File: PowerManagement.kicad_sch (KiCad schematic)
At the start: 6 parts

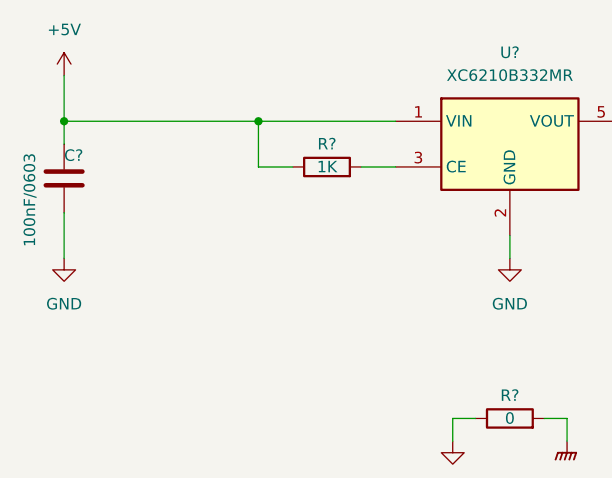
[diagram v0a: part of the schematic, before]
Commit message: Add IO sub schematic, add communications
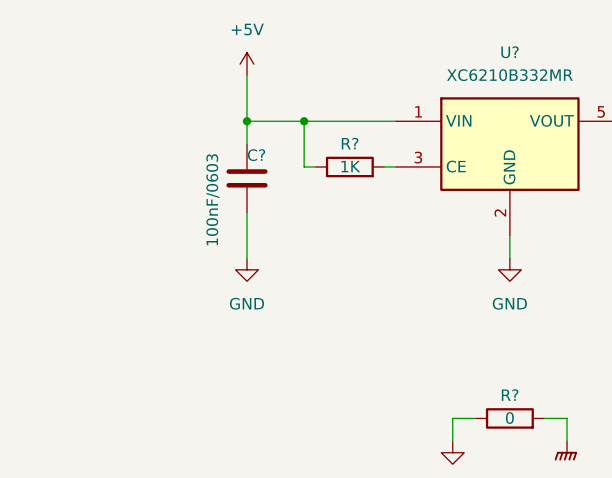
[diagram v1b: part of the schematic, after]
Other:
- moved on the sheet: C?, R?
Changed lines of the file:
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@@
   (junction (at 158.75 93.98) (diameter 0) (color 0 0 0 0)
   )
-  (junction (at 91.44 93.98) (diameter 0) (color 0 0 0 0)
-  )
-  (junction (at 113.03 93.98) (diameter 0) (color 0 0 0 0)
-  )
-  (wire (pts (xy 91.44 93.98) (xy 91.44 96.52))
-    (stroke (width 0) (type default) (color 0 0 0 0))
-  )
-  (wire (pts (xy 116.84 99.06) (xy 113.03 99.06))
+  (junction (at 111.76 93.98) (diameter 0) (color 0 0 0 0)
+  )
+  (junction (at 118.11 93.98) (diameter 0) (color 0 0 0 0)
+  )
+  (wire (pts (xy 111.76 93.98) (xy 111.76 96.52))
+    (stroke (width 0) (type default) (color 0 0 0 0))
+  )
+  (wire (pts (xy 119.38 99.06) (xy 118.11 99.06))
+    (stroke (width 0) (type default) (color 0 0 0 0))
+  )
+  (wire (pts (xy 118.11 93.98) (xy 128.27 93.98))
     (stroke (width 0) (type default) (color 0 0 0 0))
   )
@@
     (stroke (width 0) (type default) (color 0 0 0 0))
   )
-  (wire (pts (xy 113.03 99.06) (xy 113.03 93.98))
+  (wire (pts (xy 118.11 99.06) (xy 118.11 93.98))
     (stroke (width 0) (type default) (color 0 0 0 0))
   )
@@
     (stroke (width 0) (type default) (color 0 0 0 0))
   )
-  (wire (pts (xy 91.44 93.98) (xy 113.03 93.98))
-    (stroke (width 0) (type default) (color 0 0 0 0))
-  )
-  (wire (pts (xy 124.46 99.06) (xy 128.27 99.06))
+  (wire (pts (xy 111.76 93.98) (xy 118.11 93.98))
+    (stroke (width 0) (type default) (color 0 0 0 0))
+  )
+  (wire (pts (xy 127 99.06) (xy 128.27 99.06))
     (stroke (width 0) (type default) (color 0 0 0 0))
   )
@@
     (stroke (width 0) (type default) (color 0 0 0 0))
   )
-  (wire (pts (xy 113.03 93.98) (xy 128.27 93.98))
-    (stroke (width 0) (type default) (color 0 0 0 0))
-  )
   (wire (pts (xy 158.75 104.14) (xy 158.75 109.22))
     (stroke (width 0) (type default) (color 0 0 0 0))
@@
     (stroke (width 0) (type default) (color 0 0 0 0))
   )
-  (wire (pts (xy 91.44 88.9) (xy 91.44 93.98))
-    (stroke (width 0) (type default) (color 0 0 0 0))
-  )
-  (wire (pts (xy 91.44 104.14) (xy 91.44 109.22))
+  (wire (pts (xy 111.76 88.9) (xy 111.76 93.98))
+    (stroke (width 0) (type default) (color 0 0 0 0))
+  )
+  (wire (pts (xy 111.76 104.14) (xy 111.76 109.22))
     (stroke (width 0) (type default) (color 0 0 0 0))
   )
@@
     (pin "1")
   )
-  (symbol (lib_id "power:+5V") (at 91.44 88.9 0) (unit 1)
-    (in_bom yes) (on_board yes) (fields_autoplaced)
-    (property "Reference" "#PWR?" (id 0) (at 91.44 92.71 0)
-      (effects (font (size 1.27 1.27)) hide)
-    )
-    (property "Value" "+5V" (id 1) (at 91.44 83.82 0))
-    (property "Footprint" "" (id 2) (at 91.44 88.9 0)
-      (effects (font (size 1.27 1.27)) hide)
-    )
-    (property "Datasheet" "" (id 3) (at 91.44 88.9 0)
+  (symbol (lib_id "power:+5V") (at 111.76 88.9 0) (unit 1)
+    (in_bom yes) (on_board yes) (fields_autoplaced)
+    (property "Reference" "#PWR?" (id 0) (at 111.76 92.71 0)
+      (effects (font (size 1.27 1.27)) hide)
+    )
+    (property "Value" "+5V" (id 1) (at 111.76 83.82 0))
+    (property "Footprint" "" (id 2) (at 111.76 88.9 0)
+      (effects (font (size 1.27 1.27)) hide)
+    )
+    (property "Datasheet" "" (id 3) (at 111.76 88.9 0)
       (effects (font (size 1.27 1.27)) hide)
     )
@@
     (pin "2")
   )
-  (symbol (lib_id "Device:C") (at 91.44 100.33 180) (unit 1)
-    (in_bom yes) (on_board yes)
-    (property "Reference" "C?" (id 0) (at 91.44 97.79 0)
-      (effects (font (size 1.27 1.27)) (justify right))
-    )
-    (property "Value" "100nF/0603" (id 1) (at 87.63 107.95 90)
-      (effects (font (size 1.27 1.27)) (justify right))
-    )
-    (property "Footprint" "Capacitor_SMD:C_0603_1608Metric" (id 2) (at 90.4748 96.52 0)
-      (effects (font (size 1.27 1.27)) hide)
-    )
-    (property "Datasheet" "~" (id 3) (at 91.44 100.33 0)
-      (effects (font (size 1.27 1.27)) hide)
-    )
-    (pin "1")
-    (pin "2")
-  )
-  (symbol (lib_id "power:GND") (at 91.44 109.22 0) (unit 1)
-    (in_bom yes) (on_board yes) (fields_autoplaced)
-    (property "Reference" "#PWR?" (id 0) (at 91.44 115.57 0)
-      (effects (font (size 1.27 1.27)) hide)
-    )
-    (property "Value" "GND" (id 1) (at 91.44 114.3 0))
-    (property "Footprint" "" (id 2) (at 91.44 109.22 0)
-      (effects (font (size 1.27 1.27)) hide)
-    )
-    (property "Datasheet" "" (id 3) (at 91.44 109.22 0)
+  (symbol (lib_id "Device:C") (at 111.76 100.33 180) (unit 1)
+    (in_bom yes) (on_board yes)
+    (property "Reference" "C?" (id 0) (at 111.76 97.79 0)
+      (effects (font (size 1.27 1.27)) (justify right))
+    )
+    (property "Value" "100nF/0603" (id 1) (at 107.95 107.95 90)
+      (effects (font (size 1.27 1.27)) (justify right))
+    )
+    (property "Footprint" "Capacitor_SMD:C_0603_1608Metric" (id 2) (at 110.7948 96.52 0)
+      (effects (font (size 1.27 1.27)) hide)
+    )
+    (property "Datasheet" "~" (id 3) (at 111.76 100.33 0)
+      (effects (font (size 1.27 1.27)) hide)
+    )
+    (pin "1")
+    (pin "2")
+  )
+  (symbol (lib_id "power:GND") (at 111.76 109.22 0) (unit 1)
+    (in_bom yes) (on_board yes) (fields_autoplaced)
+    (property "Reference" "#PWR?" (id 0) (at 111.76 115.57 0)
+      (effects (font (size 1.27 1.27)) hide)
+    )
+    (property "Value" "GND" (id 1) (at 111.76 114.3 0))
+    (property "Footprint" "" (id 2) (at 111.76 109.22 0)
+      (effects (font (size 1.27 1.27)) hide)
+    )
+    (property "Datasheet" "" (id 3) (at 111.76 109.22 0)
       (effects (font (size 1.27 1.27)) hide)
     )
@@
     (pin "5")
   )
-  (symbol (lib_id "Device:R") (at 120.65 99.06 90) (unit 1)
-    (in_bom yes) (on_board yes)
-    (property "Reference" "R?" (id 0) (at 120.65 96.52 90))
-    (property "Value" "1K" (id 1) (at 120.65 99.06 90))
-    (property "Footprint" "Resistor_SMD:R_0603_1608Metric" (id 2) (at 120.65 100.838 90)
-      (effects (font (size 1.27 1.27)) hide)
-    )
-    (property "Datasheet" "~" (id 3) (at 120.65 99.06 0)
-      (effects (font (size 1.27 1.27)) hide)
-    )
+  (symbol (lib_id "Device:R") (at 123.19 99.06 90) (unit 1)
+    (in_bom yes) (on_board yes)
+    (property "Reference" "R?" (id 0) (at 123.19 96.52 90))
+    (property "Value" "1K" (id 1) (at 123.19 99.06 90))
+    (property "Footprint" "Resistor_SMD:R_0603_1608Metric" (id 2) (at 123.19 100.838 90)
+      (effects (font (size 1.27 1.27)) hide)
+    )
+    (property "Datasheet" "~" (id 3) (at 123.19 99.06 0)
+      (effects (font (size 1.27 1.27)) hide)
+    )

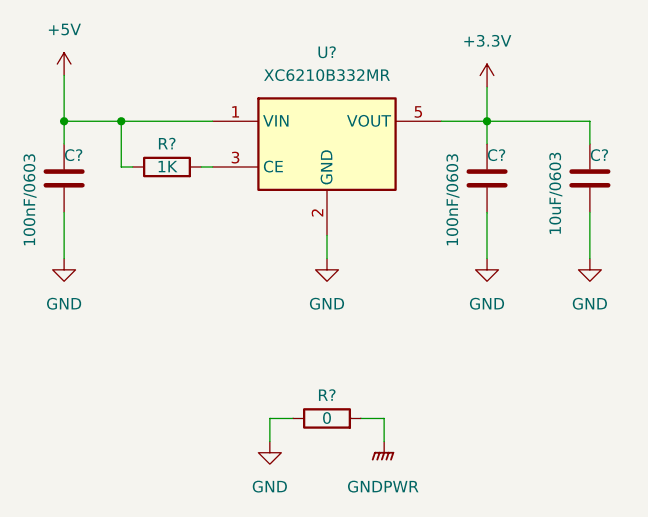
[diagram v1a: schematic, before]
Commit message: add IO, MCU, power sheets
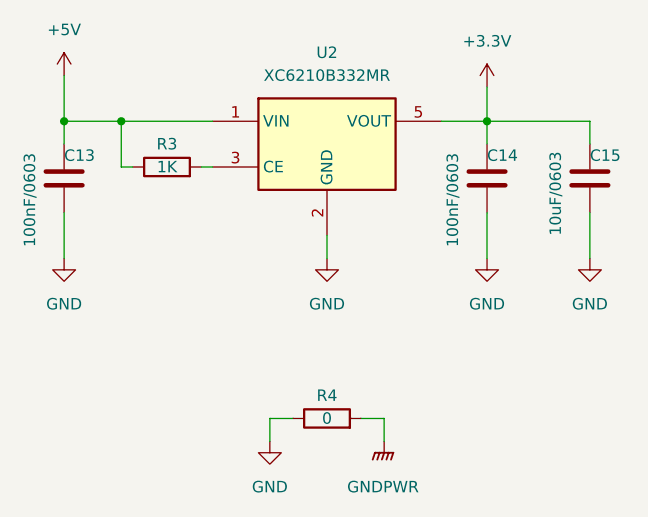
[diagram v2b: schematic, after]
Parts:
- gave numbers to parts that had none: 6

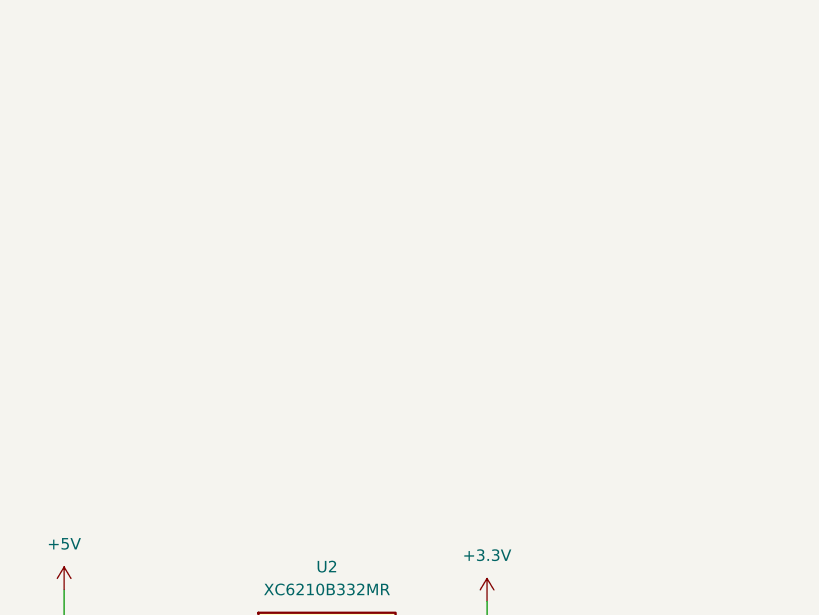
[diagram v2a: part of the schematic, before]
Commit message: Add buck converter, add part of pinmap to mcu
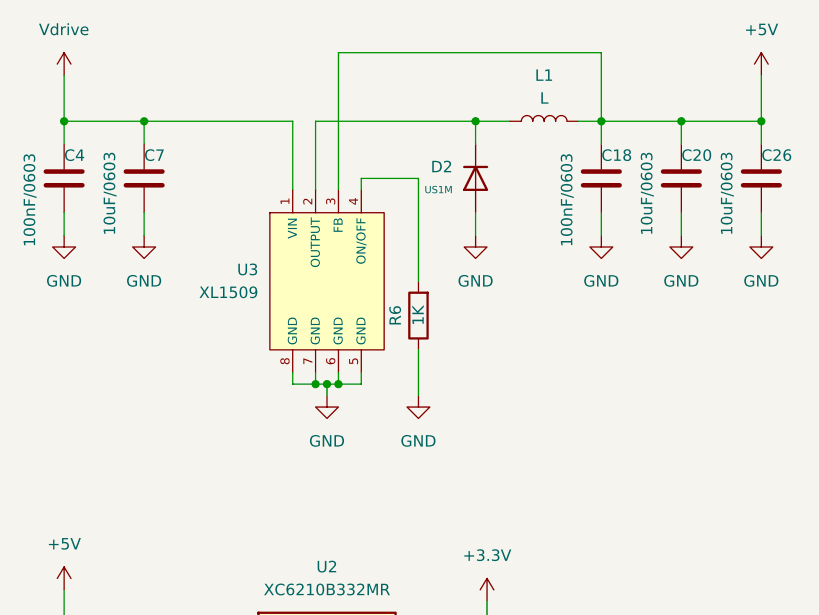
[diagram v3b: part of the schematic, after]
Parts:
- added C18, C4: 100nF/0603, Capacitor_SMD:C_0603_1608Metric, symbol Device:C
- added C20, C26, C7: 10uF/0603, Capacitor_SMD:C_0603_1608Metric, symbol Device:C
- added D2: US1M, PCM_JLCPCB:D_SMA, symbol PCM_JLCPCB-Diodes:Recovery,US1M
- added L1: L, symbol Device:L
- added R6: 1K, Resistor_SMD:R_0603_1608Metric, symbol Device:R
- added U3: XL1509, PCM_JLCPCB:SOIC-8_L5.0-W4.0-P1.27-LS6.0-BL, symbol PCM_JLCPCB-Power:DC-DC, Buck, 4-40VIN, 2A, 5VOUT
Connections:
- net +5V: now also C18.2, C20.2, C26.2, L1.2, U3.3 (FB)
- net GND: now also C18.1, C20.1, C26.1, C4.1, C7.1, D2.2, R6.1, U3.5 (GND), U3.6 (GND), U3.7 (GND), U3.8 (GND)
- new net: R6.2, U3.4 (ON/OFF)
- new net: D2.1, L1.1, U3.2 (OUTPUT)
- new net Vdrive: C4.2, C7.2, U3.1 (VIN)

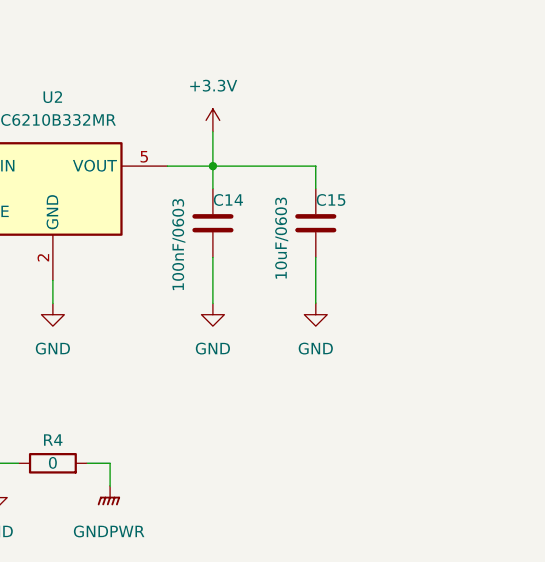
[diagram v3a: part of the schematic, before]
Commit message: Add mcu connections
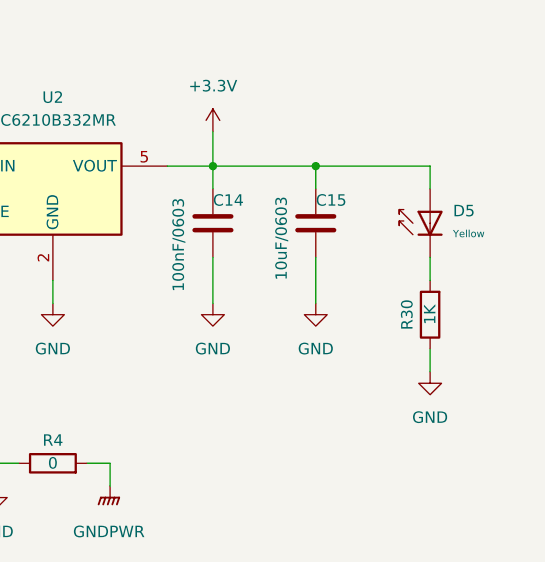
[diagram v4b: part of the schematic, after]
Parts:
- added D5: Yellow, PCM_JLCPCB:D_0603, symbol PCM_JLCPCB-Diodes:LED,0603,Yellow
- added R30: 1K, Resistor_SMD:R_0603_1608Metric, symbol Device:R
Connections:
- net +3.3V: now also D5.2
- net GND: now also R30.1
- new net: D5.1, R30.2

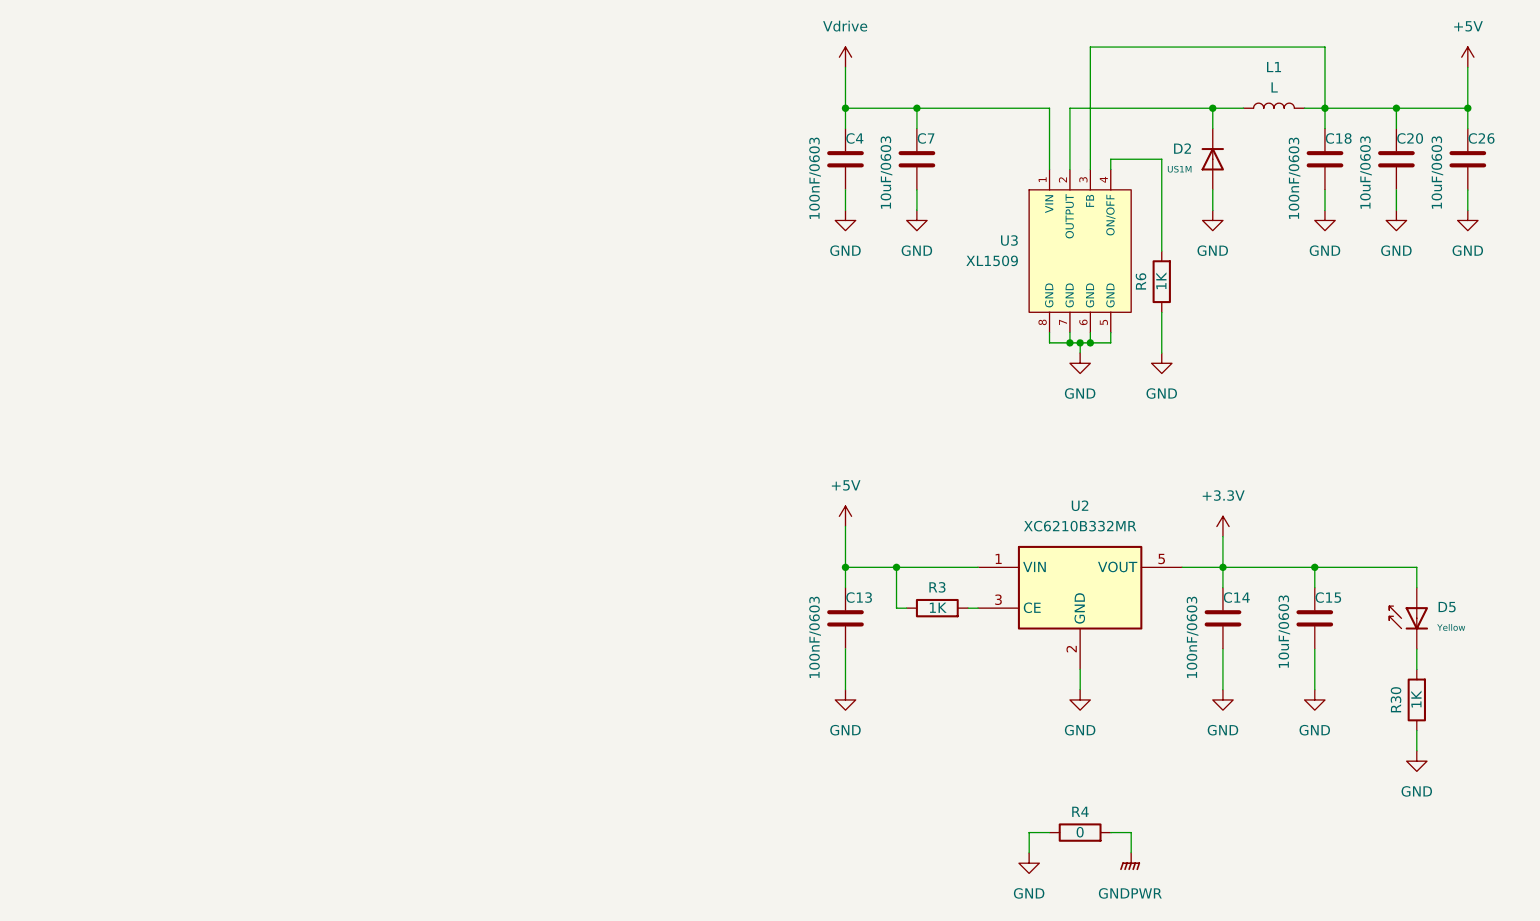
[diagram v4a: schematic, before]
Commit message: Added DRV layout
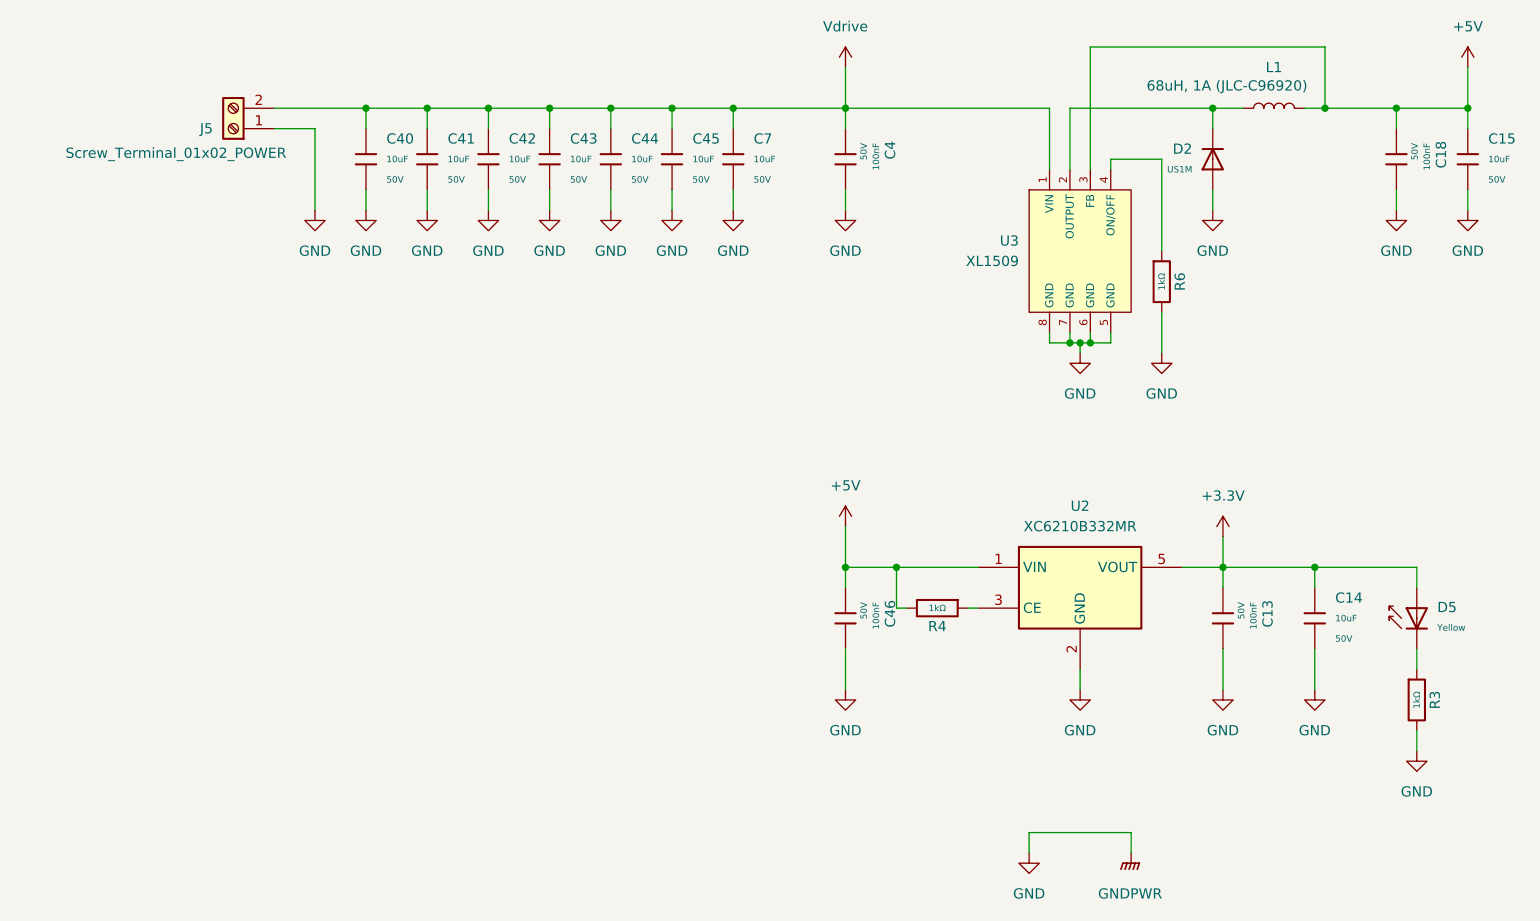
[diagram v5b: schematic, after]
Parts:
- removed C13, C14, C18, C4: 100nF/0603, Capacitor_SMD:C_0603_1608Metric, symbol Device:C
- removed C15, C20, C26, C7: 10uF/0603, Capacitor_SMD:C_0603_1608Metric, symbol Device:C
- removed R3, R30, R6: 1K, Resistor_SMD:R_0603_1608Metric, symbol Device:R
- removed R4: 0, Resistor_SMD:R_0603_1608Metric, symbol Device:R
- added C13, C18, C4, C46: 100nF, PCM_JLCPCB:C_0603, symbol PCM_JLCPCB-Capacitors:0603,100nF
- added C14, C15, C40, C41, C42, C43, C44, C45, C7: 10uF, PCM_JLCPCB:C_1206, symbol PCM_JLCPCB-Capacitors:1206,10uF
- added J5: Screw_Terminal_01x02_POWER, Connector_Phoenix_MC:PhoenixContact_MC_1,5_2-G-3.5_1x02_P3.50mm_Horizontal, symbol Connector:Screw_Terminal_01x02
- added R3, R4, R6: 1kΩ, PCM_JLCPCB:R_0603, symbol PCM_JLCPCB-Resistors:0603,1kΩ
- L1: value L -> 68uH, 1A (JLC-C96920); footprint (none) -> Inductor_SMD:L_Changjiang_FNR5020S
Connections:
- net +3.3V: now also C13.1, C14.1
- net +5V: now also C15.1, C18.1, C46.1, R4.2
- net GND: now also C13.2, C14.2, C15.2, C18.2, C4.2, C40.2, C41.2, C42.2, C43.2, C44.2, C45.2, C46.2, C7.2, J5.1 (Pin_1), R3.2, R6.2
- net Vdrive: now also C4.1, C40.1, C41.1, C42.1, C43.1, C44.1, C45.1, C7.1, J5.2 (Pin_2)
- net at D5.1: now also R3.1
- net at U3.4 (ON/OFF): now also R6.1
- net at U2.3 (CE): now also R4.1
